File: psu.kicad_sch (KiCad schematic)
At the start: 4 parts

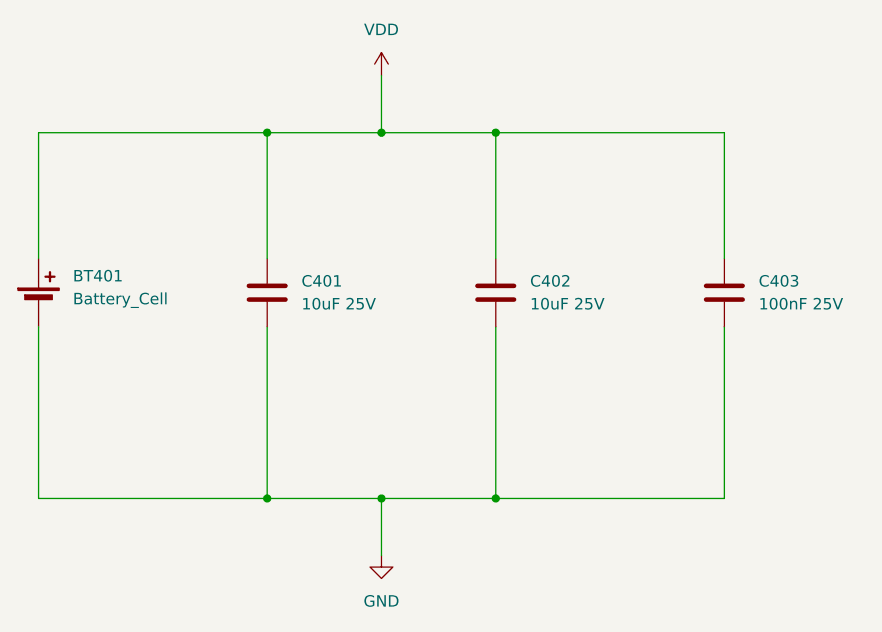
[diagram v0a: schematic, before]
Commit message: Update Schematics - Add footprint to symbols.
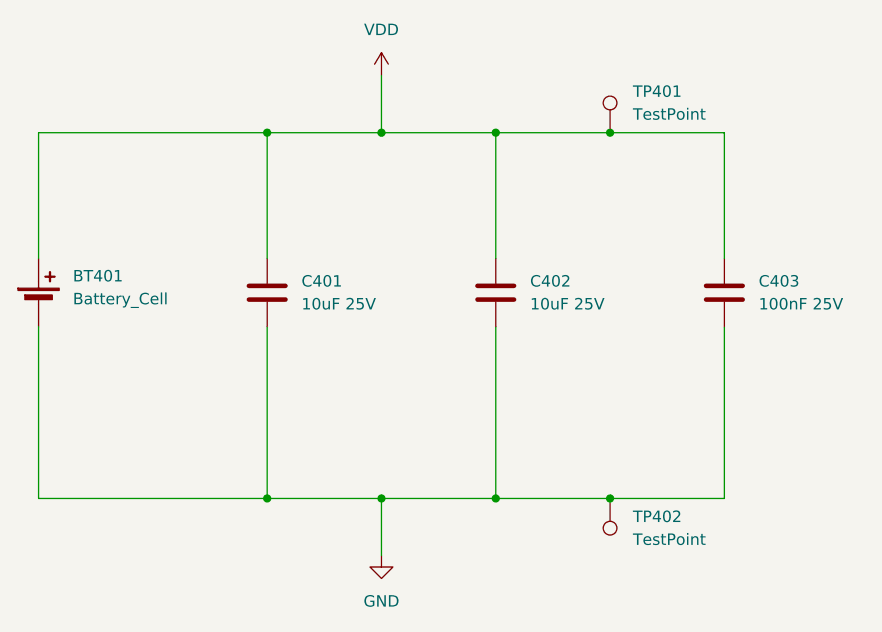
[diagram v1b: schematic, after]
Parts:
- added TP401, TP402: TestPoint, TestPoint:TestPoint_Keystone_5005-5009_Compact, symbol Connector:TestPoint
- BT401: footprint (none) -> Battery:BatteryHolder_Keystone_1058_1x2032
- C401, C402: footprint (none) -> Capacitor_SMD:C_0603_1608Metric
- C403: footprint (none) -> Capacitor_SMD:C_0402_1005Metric
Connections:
- net GND: now also TP402.1
- net VDD: now also TP401.1
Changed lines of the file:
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@@
+	)
+	(junction
+		(at 114.3 91.44)
+		(diameter 0)
+		(color 0 0 0 0)
 	)
 	(junction
@@
 	)
 	(junction
+		(at 114.3 50.8)
+		(diameter 0)
+		(color 0 0 0 0)
+	)
+	(junction
 		(at 101.6 50.8)
 		(diameter 0)
@@
 	(wire
 		(pts
+			(xy 114.3 50.8) (xy 127 50.8)
+		)
+		(stroke
+			(width 0)
+			(type default)
+		)
+	)
+	(wire
+		(pts
 			(xy 88.9 44.45) (xy 88.9 50.8)
 		)
@@
 	(wire
 		(pts
-			(xy 127 91.44) (xy 101.6 91.44)
+			(xy 127 91.44) (xy 114.3 91.44)
 		)
 		(stroke
@@
 	(wire
 		(pts
-			(xy 101.6 50.8) (xy 127 50.8)
+			(xy 101.6 50.8) (xy 114.3 50.8)
 		)
 		(stroke
@@
 		(pts
 			(xy 50.8 64.77) (xy 50.8 50.8)
+		)
+		(stroke
+			(width 0)
+			(type default)
+		)
+	)
+	(wire
+		(pts
+			(xy 114.3 91.44) (xy 101.6 91.44)
 		)
 		(stroke
@@
 			)
 		)
-		(property "Footprint" ""
+		(property "Footprint" "Capacitor_SMD:C_0402_1005Metric"
 			(at 127.9652 72.39 0)
 			(effects
@@
 				(path "/0fb6cf8e-df3c-4656-9a7e-f74b2436dafb/10bbb489-5c93-4b16-8e6f-ed980d178bf1"
 					(reference "C403")
+					(unit 1)
+				)
+			)
+		)
+	)
+	(symbol
+		(lib_id "Connector:TestPoint")
+		(at 114.3 50.8 0)
+		(unit 1)
+		(exclude_from_sim no)
+		(in_bom yes)
+		(on_board yes)
+		(dnp no)
+		(fields_autoplaced yes)
+		(property "Reference" "TP401"
+			(at 116.84 46.2279 0)
+			(effects
+				(font
+					(size 1.27 1.27)
+				)
+				(justify left)
+			)
+		)
+		(property "Value" "TestPoint"
+			(at 116.84 48.7679 0)
+			(effects
+				(font
+					(size 1.27 1.27)
+				)
+				(justify left)
+			)
+		)
+		(property "Footprint" "TestPoint:TestPoint_Keystone_5005-5009_Compact"
+			(at 119.38 50.8 0)
+			(effects
+				(font
+					(size 1.27 1.27)
+				)
+				(hide yes)
+			)
+		)
+		(property "Datasheet" "~"
+			(at 119.38 50.8 0)
+			(effects
+				(font
+					(size 1.27 1.27)
+				)
+				(hide yes)
+			)
+		)
+		(property "Description" "test point"
+			(at 114.3 50.8 0)
+			(effects
+				(font
+					(size 1.27 1.27)
+				)
+				(hide yes)
+			)
+		)
+		(pin "1"
+		)
+		(instances
+			(project ""
+				(path "/0fb6cf8e-df3c-4656-9a7e-f74b2436dafb/10bbb489-5c93-4b16-8e6f-ed980d178bf1"
+					(reference "TP401")
 					(unit 1)
 				)
@@
 			)
 		)
-		(property "Footprint" ""
+		(property "Footprint" "Battery:BatteryHolder_Keystone_1058_1x2032"
 			(at 50.8 68.326 90)
 			(effects
@@
 			)
 		)
-		(property "Footprint" ""
+		(property "Footprint" "Capacitor_SMD:C_0603_1608Metric"
 			(at 77.1652 72.39 0)
 			(effects
@@
 				(path "/0fb6cf8e-df3c-4656-9a7e-f74b2436dafb/10bbb489-5c93-4b16-8e6f-ed980d178bf1"
 					(reference "C401")
+					(unit 1)
+				)
+			)
+		)
+	)
+	(symbol
+		(lib_id "Connector:TestPoint")
+		(at 114.3 91.44 180)
+		(unit 1)
+		(exclude_from_sim no)
+		(in_bom yes)
+		(on_board yes)
+		(dnp no)
+		(fields_autoplaced yes)
+		(property "Reference" "TP402"
+			(at 116.84 93.4719 0)
+			(effects
+				(font
+					(size 1.27 1.27)
+				)
+				(justify right)
+			)
+		)
+		(property "Value" "TestPoint"
+			(at 116.84 96.0119 0)
+			(effects
+				(font
+					(size 1.27 1.27)
+				)
+				(justify right)
+			)
+		)
+		(property "Footprint" "TestPoint:TestPoint_Keystone_5005-5009_Compact"
+			(at 109.22 91.44 0)
+			(effects
+				(font
+					(size 1.27 1.27)
+				)
+				(hide yes)
+			)
+		)
+		(property "Datasheet" "~"
+			(at 109.22 91.44 0)
+			(effects
+				(font
+					(size 1.27 1.27)
+				)
+				(hide yes)
+			)
+		)
+		(property "Description" "test point"
+			(at 114.3 91.44 0)
+			(effects
+				(font
+					(size 1.27 1.27)
+				)
+				(hide yes)
+			)
+		)
+		(pin "1"
+		)
+		(instances
+			(project "GreenHAir_Node"
+				(path "/0fb6cf8e-df3c-4656-9a7e-f74b2436dafb/10bbb489-5c93-4b16-8e6f-ed980d178bf1"
+					(reference "TP402")
 					(unit 1)
 				)
@@
 			)
 		)
-		(property "Footprint" ""
+		(property "Footprint" "Capacitor_SMD:C_0603_1608Metric"
 			(at 102.5652 72.39 0)
 			(effects
